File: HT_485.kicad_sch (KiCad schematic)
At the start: 41 parts, among them J1 POWER, J2 485, SW1 EDS05SGRSTR04Q, U1 ISL3179EIBZ, U2 SHT31-DIS-P2.5KS, U3 LM2576D2TR4-3.3G, U4 STM32L010F4P6

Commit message: Adattato master a scatola
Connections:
- net 485+: now also J2.1 (Pin_1); no longer J2.2 (Pin_2)
- net 485-: now also J2.2 (Pin_2); no longer J2.1 (Pin_1)
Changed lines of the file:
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@@
+    (stroke (width 0) (type default) (color 0 0 0 0))
+  )
+  (wire (pts (xy 273.05 132.08) (xy 287.02 132.08))
+    (stroke (width 0) (type default) (color 0 0 0 0))
+  )
+  (wire (pts (xy 125.73 163.83) (xy 125.73 166.37))
+    (stroke (width 0) (type default) (color 0 0 0 0))
+  )
+  (wire (pts (xy 57.15 39.37) (xy 57.15 46.99))
+    (stroke (width 0) (type default) (color 0 0 0 0))
+  )
+  (wire (pts (xy 300.99 119.38) (xy 312.42 119.38))
+    (stroke (width 0) (type default) (color 0 0 0 0))
+  )
+  (wire (pts (xy 189.23 171.45) (xy 189.23 166.37))
+    (stroke (width 0) (type default) (color 0 0 0 0))
+  )
+  (wire (pts (xy 273.05 109.22) (xy 285.75 109.22))
     (stroke (width 0) (type default) (color 0 0 0 0))
   )
   (wire (pts (xy 151.13 119.38) (xy 151.13 124.46))
-    (stroke (width 0) (type default) (color 0 0 0 0))
-  )
-  (wire (pts (xy 273.05 132.08) (xy 287.02 132.08))
-    (stroke (width 0) (type default) (color 0 0 0 0))
-  )
-  (wire (pts (xy 125.73 163.83) (xy 125.73 166.37))
-    (stroke (width 0) (type default) (color 0 0 0 0))
-  )
-  (wire (pts (xy 57.15 39.37) (xy 57.15 46.99))
-    (stroke (width 0) (type default) (color 0 0 0 0))
-  )
-  (wire (pts (xy 300.99 119.38) (xy 312.42 119.38))
-    (stroke (width 0) (type default) (color 0 0 0 0))
-  )
-  (wire (pts (xy 189.23 171.45) (xy 189.23 166.37))
-    (stroke (width 0) (type default) (color 0 0 0 0))
-  )
-  (wire (pts (xy 273.05 109.22) (xy 285.75 109.22))
     (stroke (width 0) (type default) (color 0 0 0 0))
   )
@@
     (pin "2")
   )
-  (symbol (lib_id "Connector:Conn_01x02_Female") (at 156.21 119.38 0) (mirror x) (unit 1)
-    (in_bom yes) (on_board yes) (fields_autoplaced)
-    (property "Reference" "J2" (id 0) (at 155.575 111.76 0))
-    (property "Value" "485" (id 1) (at 155.575 114.3 0))
-    (property "Footprint" "TerminalBlock_Phoenix:TerminalBlock_Phoenix_PT-1,5-2-3.5-H_1x02_P3.50mm_Horizontal" (id 2) (at 156.21 119.38 0)
-      (effects (font (size 1.27 1.27)) hide)
-    )
-    (property "Datasheet" "~" (id 3) (at 156.21 119.38 0)
-      (effects (font (size 1.27 1.27)) hide)
-    )
+  (symbol (lib_id "Connector:Conn_01x02_Female") (at 156.21 116.84 0) (unit 1)
+    (in_bom yes) (on_board yes) (fields_autoplaced)
+    (property "Reference" "J2" (id 0) (at 157.48 116.8399 0)
+      (effects (font (size 1.27 1.27)) (justify left))
+    )
+    (property "Value" "485" (id 1) (at 157.48 119.3799 0)
+      (effects (font (size 1.27 1.27)) (justify left))
+    )
+    (property "Footprint" "TerminalBlock_Phoenix:TerminalBlock_Phoenix_PT-1,5-2-3.5-H_1x02_P3.50mm_Horizontal" (id 2) (at 156.21 116.84 0)
+      (effects (font (size 1.27 1.27)) hide)
+    )
+    (property "Datasheet" "~" (id 3) (at 156.21 116.84 0)
+      (effects (font (size 1.27 1.27)) hide)
+    )

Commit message: Aggiunto terminatore 485
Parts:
- added R20: 120R, Resistor_SMD:R_0805_2012Metric_Pad1.20x1.40mm_HandSolder, symbol Device:R_Small
- added R21, R22: 370R, Resistor_SMD:R_0805_2012Metric_Pad1.20x1.40mm_HandSolder, symbol Device:R_Small
- added SW2: 416131160803, Button_Switch_SMD:SW_DIP_SPSTx03_Slide_KingTek_DSHP03TS_W7.62mm_P1.27mm, symbol Switch:SW_DIP_x03
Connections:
- net +3V3: now also R21.1
- net 485+: now also R20.1, SW2.1, SW2.3
- net 485-: now also R20.2, SW2.2, SW2.4
- net GND: now also R22.2
- new net: R22.1, SW2.5
- new net: R21.2, SW2.6

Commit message: Rivisti dip switch con solder jumper
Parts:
- removed SW1: EDS05SGRSTR04Q, Button_Switch_SMD:SW_DIP_SPSTx05_Slide_KingTek_DSHP05TJ_W5.25mm_P1.27mm_JPin, symbol Switch:SW_DIP_x05
- removed SW2: 416131160803, Button_Switch_SMD:SW_DIP_SPSTx03_Slide_KingTek_DSHP03TS_W7.62mm_P1.27mm, symbol Switch:SW_DIP_x03
- added JP1: BIAS+, Jumper:SolderJumper-2_P1.3mm_Open_RoundedPad1.0x1.5mm, symbol Jumper:SolderJumper_2_Open
- added JP2: BIAS-, Jumper:SolderJumper-2_P1.3mm_Open_RoundedPad1.0x1.5mm, symbol Jumper:SolderJumper_2_Open
- added JP3: TERMINATOR, Jumper:SolderJumper-2_P1.3mm_Open_RoundedPad1.0x1.5mm, symbol Jumper:SolderJumper_2_Open
- added JP4: A1, Jumper:SolderJumper-2_P1.3mm_Open_RoundedPad1.0x1.5mm, symbol Jumper:SolderJumper_2_Open
- added JP5: A3, Jumper:SolderJumper-2_P1.3mm_Open_RoundedPad1.0x1.5mm, symbol Jumper:SolderJumper_2_Open
- added JP6: A5, Jumper:SolderJumper-2_P1.3mm_Open_RoundedPad1.0x1.5mm, symbol Jumper:SolderJumper_2_Open
- added JP7: A2, Jumper:SolderJumper-2_P1.3mm_Open_RoundedPad1.0x1.5mm, symbol Jumper:SolderJumper_2_Open
- added JP8: A4, Jumper:SolderJumper-2_P1.3mm_Open_RoundedPad1.0x1.5mm, symbol Jumper:SolderJumper_2_Open
- R20: value 120R -> 370R
- R22: value 370R -> 120R
- U2: value SHT31-DIS-P2.5KS -> SHT31-DIS + SF2; footprint Sensor_Humidity:Sensirion_DFN-8-1EP_2.5x2.5mm_P0.5mm_EP1.1x1.7mm -> HT485:Sensirion_DFN-8-1EP_2.5x2.5mm_P0.5mm_EP1.1x1.7mm
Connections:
- net +3V3: now also R20.1; no longer R21.1
- net 485+: now also JP1.1 (A), JP3.2 (B); no longer R20.1
- net 485-: now also R22.2, JP2.1 (A); no longer R20.2
- net GND: now also R21.2, JP4.2 (B), JP5.2 (B), JP6.2 (B), JP7.2 (B), JP8.2 (B); no longer R22.2
- net at R12.1, R17.2: now also JP8.1 (A)
- net at R22.1: now also JP3.1 (A)
- net at R13.1, R18.2: now also JP6.1 (A)
- net at R11.1, R16.2: now also JP5.1 (A)
- net at R14.2, R9.1: now also JP4.1 (A)
- net at R10.1, R15.2: now also JP7.1 (A)
- new net: JP1.2 (B), R20.2
- new net: JP2.2 (B), R21.1

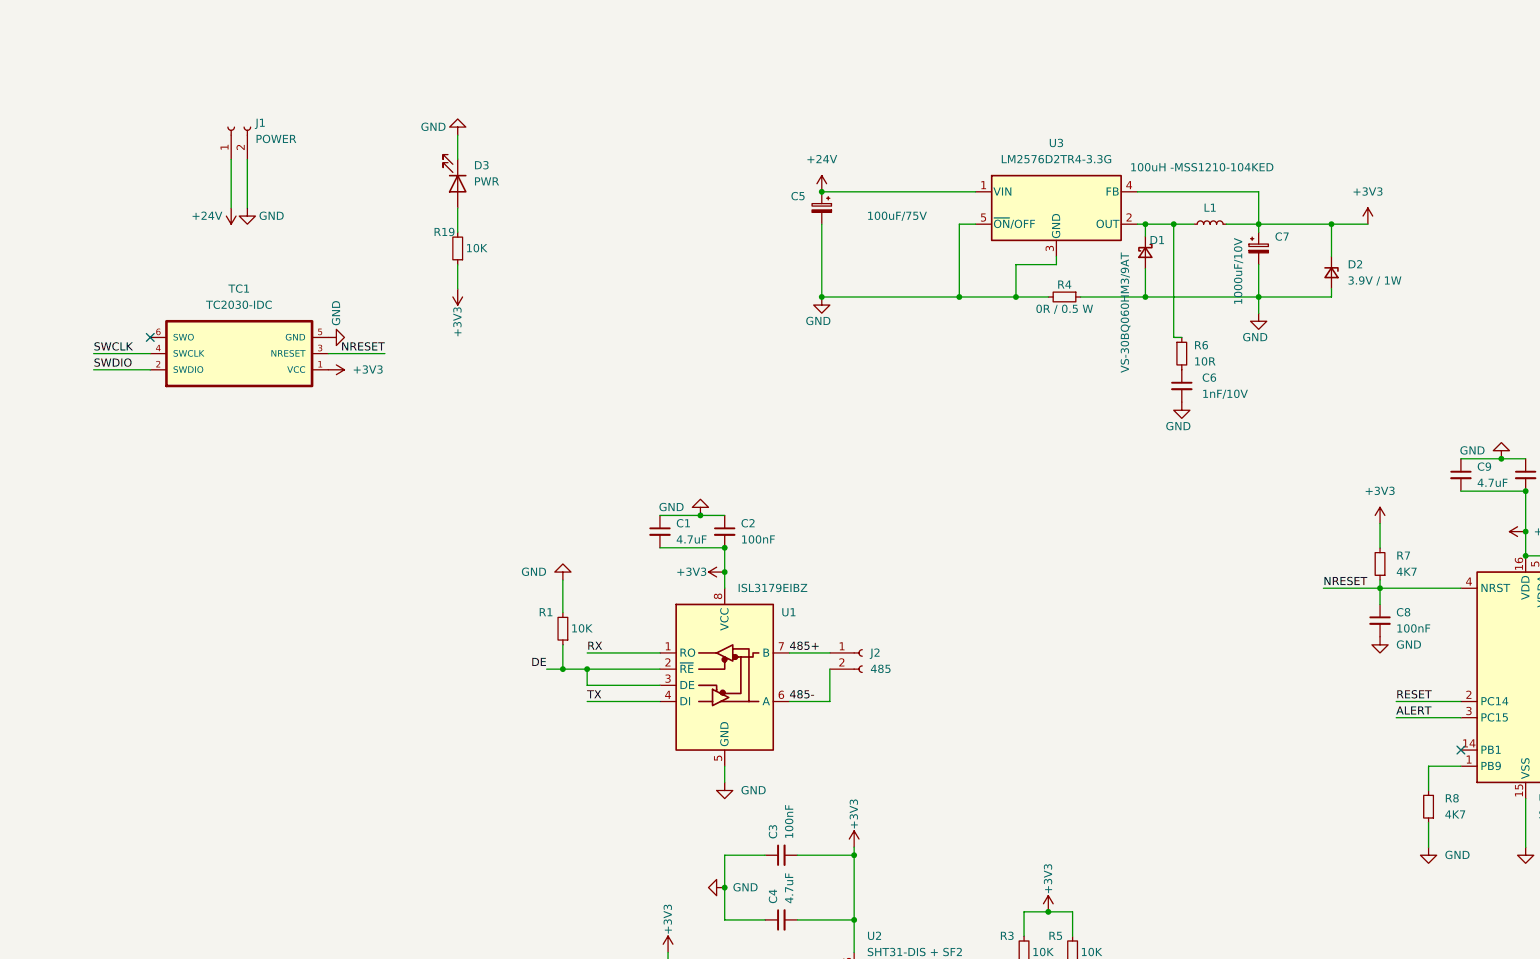
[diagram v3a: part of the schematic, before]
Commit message: Messa pompa di carica per 485 a 5V
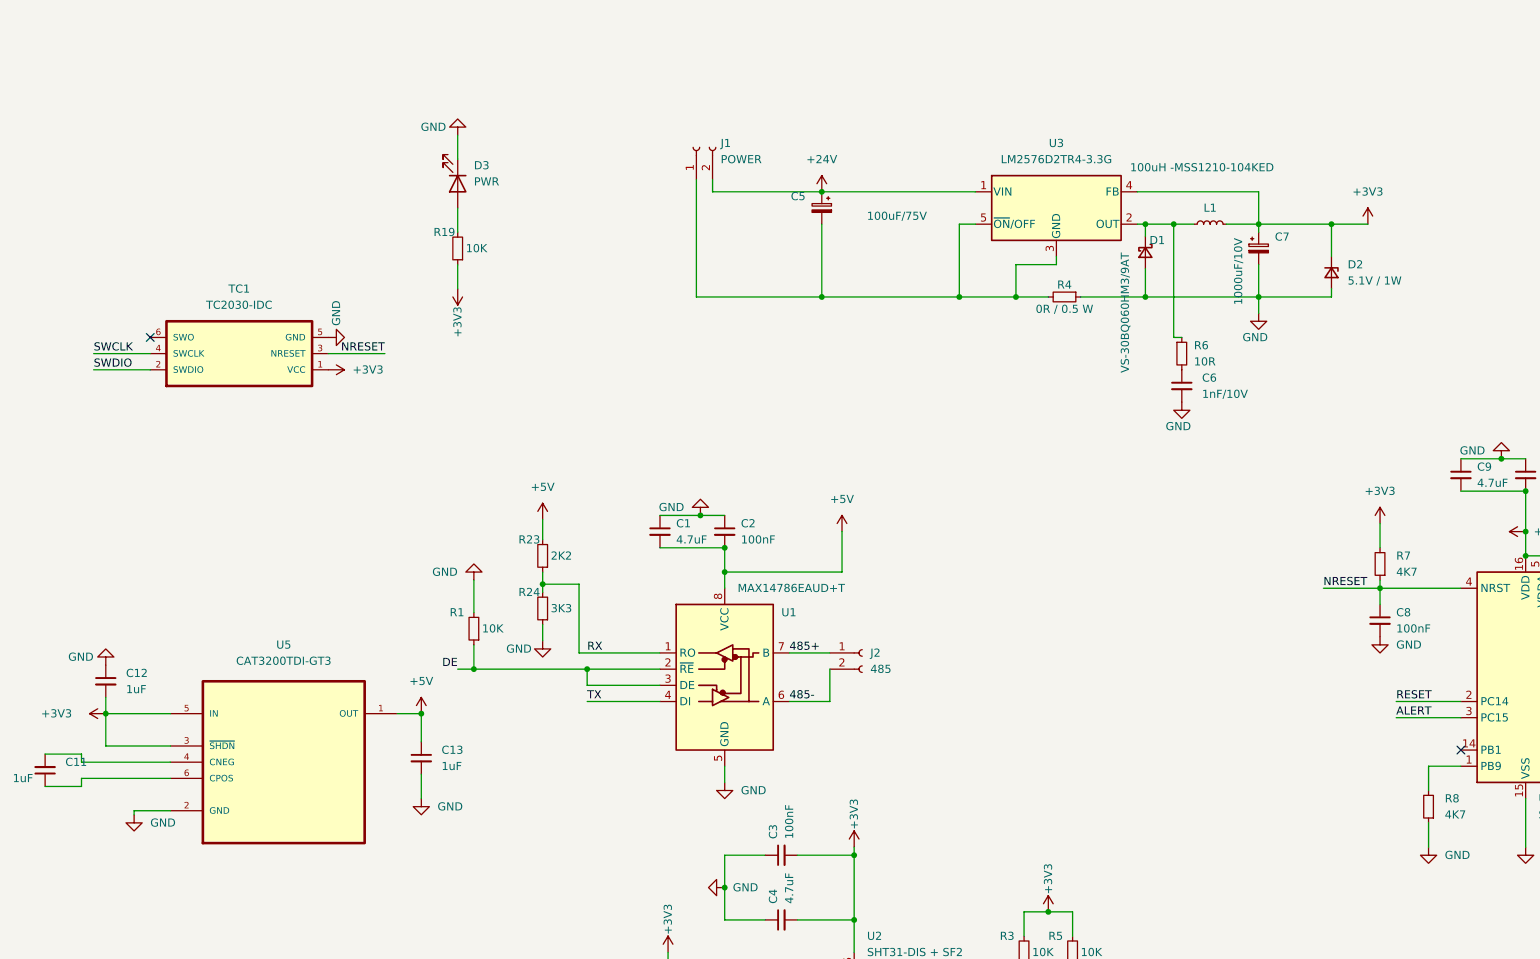
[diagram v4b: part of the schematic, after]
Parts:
- added C11, C12, C13: 1uF, Capacitor_SMD:C_0805_2012Metric_Pad1.18x1.45mm_HandSolder, symbol Device:C_Small
- added R23: 2K2, Resistor_SMD:R_0805_2012Metric_Pad1.20x1.40mm_HandSolder, symbol Device:R_Small
- added R24: 3K3, Resistor_SMD:R_0805_2012Metric_Pad1.20x1.40mm_HandSolder, symbol Device:R_Small
- added U5: CAT3200TDI-GT3, Package_TO_SOT_SMD:TSOT-23-6, symbol HT485:CAT3200TDI-GT3
- D2: value 3.9V / 1W -> 5.1V / 1W
- U1: value ISL3179EIBZ -> MAX14786EAUD+T
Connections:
- net +24V: now also J1.2 (Pin_2); no longer J1.1 (Pin_1)
- net +3V3: now also C12.2, U5.3 (~{SHDN}), U5.5 (IN); no longer C1.2, C2.2, U1.8 (VCC)
- net GND: now also C12.1, C13.2, R24.1, U5.2 (GND); no longer C5.2, J1.2 (Pin_2), R4.2, U3.3 (GND), U3.5 (~{ON}/OFF)
- net RX: now also R23.1, R24.2
- new net: C5.2, J1.1 (Pin_1), R4.2, U3.3 (GND), U3.5 (~{ON}/OFF)
- new net: C11.1, U5.6 (CPOS)
- new net: C11.2, U5.4 (CNEG)
- new net +5V: C1.2, C13.1, C2.2, R23.2, U1.8 (VCC), U5.1 (OUT)
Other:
- moved on the sheet: J1, R1

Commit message: Revisione 1.0.0.0 con PT1000
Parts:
- removed C10: 100nF, Capacitor_SMD:C_0805_2012Metric_Pad1.18x1.45mm_HandSolder, symbol Device:C_Small
- removed JP4: A1, Jumper:SolderJumper-2_P1.3mm_Open_RoundedPad1.0x1.5mm, symbol Jumper:SolderJumper_2_Open
- removed JP5: A3, Jumper:SolderJumper-2_P1.3mm_Open_RoundedPad1.0x1.5mm, symbol Jumper:SolderJumper_2_Open
- removed JP6: A5, Jumper:SolderJumper-2_P1.3mm_Open_RoundedPad1.0x1.5mm, symbol Jumper:SolderJumper_2_Open
- removed JP7: A2, Jumper:SolderJumper-2_P1.3mm_Open_RoundedPad1.0x1.5mm, symbol Jumper:SolderJumper_2_Open
- removed JP8: A4, Jumper:SolderJumper-2_P1.3mm_Open_RoundedPad1.0x1.5mm, symbol Jumper:SolderJumper_2_Open
- removed TC1: TC2030-IDC, TC2030:TC2030-IDC, symbol TC2030:TC2030-IDC
- removed U2: SHT31-DIS + SF2, HT485:Sensirion_DFN-8-1EP_2.5x2.5mm_P0.5mm_EP1.1x1.7mm, symbol Sensor_Humidity:SHT31-DIS
- removed U4: STM32L010F4P6, Package_SO:TSSOP-20_4.4x6.5mm_P0.65mm, symbol MCU_ST_STM32L0:STM32L011F3Px
- added C14, C15, C20: 100nF, Capacitor_SMD:C_0805_2012Metric, symbol Device:C_Small
- added C16: 1nF, Capacitor_SMD:C_0805_2012Metric, symbol Device:C_Small
- added C17: 1uF/25V, Capacitor_SMD:C_0805_2012Metric, symbol Device:C_Small
- added C18, C19: 100uF/25V, Capacitor_SMD:CP_Elec_6.3x7.7, symbol Device:C_Polarized_Small
- added D10: STPS0520Z, Diode_SMD:D_SOD-123, symbol Device:D_Schottky_Small
- added D4, D5, D6, D7, D8: 1N4148WS, Diode_SMD:D_SOD-323, symbol Diode:1N4148WS
- added D9: BAV99, Package_TO_SOT_SMD:SOT-23, symbol Diode:BAV99
- added J3: PT1000, TerminalBlock_Phoenix:TerminalBlock_Phoenix_PT-1,5-2-3.5-H_1x02_P3.50mm_Horizontal, symbol Connector:Conn_01x02_Female
- added J4: H/T Sensor, Connector_JST:JST_PH_S6B-PH-SM4-TB_1x06-1MP_P2.00mm_Horizontal, symbol Connector:Conn_01x06_Female
- added J5: PRG, Connector_PinSocket_2.54mm:PinSocket_2x03_P2.54mm_Vertical, symbol Connector_Generic:Conn_02x03_Odd_Even
- added JP4: UART_BOOT_MSG, Jumper:SolderJumper-3_P1.3mm_Bridged12_RoundedPad1.0x1.5mm_NumberLabels, symbol Jumper:SolderJumper_3_Bridged12
- added Q1, Q2, Q3, Q4: BC817, Package_TO_SOT_SMD:SOT-23, symbol Transistor_BJT:BC817
- added R25, R26, R27, R30, R31: 10K, Resistor_SMD:R_0805_2012Metric_Pad1.20x1.40mm_HandSolder, symbol Device:R_Small
- added R28, R29: 0R, Resistor_SMD:R_0805_2012Metric_Pad1.20x1.40mm_HandSolder, symbol Device:R_Small
- added TP1: D+, TestPoint:TestPoint_Pad_D1.0mm, symbol Connector:TestPoint
- added TP2: D-, TestPoint:TestPoint_Pad_D1.0mm, symbol Connector:TestPoint
- added U2: TL082, Package_SO:SOIC-8-1EP_3.9x4.9mm_P1.27mm_EP2.29x3mm, symbol Amplifier_Operational:TL082
- added U4: ESP32-S3-WROOM-1-N16R8, Espressif:ESP32-S3-WROOM-1, symbol Espressif:ESP32-S3-WROOM-1
- added U6: L7815, Package_TO_SOT_SMD:TO-263-2, symbol Regulator_Linear:L7815
- C1, C11, C12, C13, C2, C8: footprint Capacitor_SMD:C_0805_2012Metric_Pad1.18x1.45mm_HandSolder -> Capacitor_SMD:C_0805_2012Metric
- C3: value 100nF -> 1uF/16V; footprint Capacitor_SMD:C_0805_2012Metric_Pad1.18x1.45mm_HandSolder -> Capacitor_SMD:C_0805_2012Metric
- C4: value 4.7uF -> 100nF; footprint Capacitor_SMD:C_0805_2012Metric_Pad1.18x1.45mm_HandSolder -> Capacitor_SMD:C_0805_2012Metric
- C5: value 100uF/75V -> 100uF / 50V; footprint Capacitor_SMD:CP_Elec_10x10 -> Capacitor_SMD:CP_Elec_8x10.5
- C9: value 4.7uF -> 10uF; footprint Capacitor_SMD:C_0805_2012Metric_Pad1.18x1.45mm_HandSolder -> Capacitor_SMD:C_0805_2012Metric
- D2: value 5.1V / 1W -> 3.9V/1W; footprint Diode_SMD:D_SOD-128 -> Diode_SMD:D_SMA
- R10: value 1K -> 100R
- R11: value 1K -> 10K
- R15: value 10K -> 1K
- R16: value 10K -> 10R
- R17: value 10K -> 3k3
- R2: value 10K -> 1K 1%
- R23: value 2K2 -> 4K7
- R24: value 3K3 -> 10K
- R7, R8: value 4K7 -> 10K
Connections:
- net +24V: now also U6.1 (IN)
- net +3V3: now also C8.1, C9.1, R23.2, D9.2 (A), J4.1 (Pin_1), J5.1 (Pin_1), R26.2, R27.2, R31.1, U4.2 (3V3); no longer C3.2, C4.2, C9.2, R14.1, R15.1, R16.1, R17.1, R18.1, R2.2, R3.2, R5.2
- net +5V: no longer R23.2
- net 485+: now also J2.2 (Pin_2); no longer J2.1 (Pin_1)
- net 485-: now also J2.1 (Pin_1); no longer J2.2 (Pin_2)
- net ALERT: now also J4.5 (Pin_5), U4.15 (GPIO3/TOUCH3/ADC1_CH2)
- net DE: now also U4.4 (GPIO4/TOUCH4/ADC1_CH3)
- net GND: now also C3.2, C4.2, C9.2, R13.2, R16.2, R5.2, C14.2, C15.2, C19.1, C20.2, D5.2 (A), D9.1 (K), J3.2 (Pin_2), J4.6 (Pin_6), J5.6 (Pin_6), Q1.2 (E), R25.2, R30.2, U4.1 (GND), U4.40 (GND), U4.41 (GND); no longer C3.1, C4.1, C9.1, R24.1, R8.1
- net RESET: now also J4.4 (Pin_4), U4.38 (GPIO2/TOUCH2/ADC1_CH1); no longer R2.1
- net RX: now also D10.2 (A), U4.11 (GPIO18/U1RXD/ADC2_CH7/CLK_OUT3); no longer R24.2, U1.1 (RO)
- net SCL: now also J4.2 (Pin_2), R26.1, U4.25 (GPIO48/SPICLK_N/SUBSPICLK_N_DIFF); no longer R5.1
- net SDA: now also J4.3 (Pin_3), R27.1, U4.24 (GPIO47/SPICLK_P/SUBSPICLK_P_DIFF); no longer R3.1
- net TX: now also U4.10 (GPIO17/U1TXD/ADC2_CH6)
- net at R8.2: now also Q3.1 (B)
- net at R10.2: now also C16.2
- net at R11.2: now also D6.1 (K), Q1.3 (C), Q2.1 (B)
- net at R12.2: now also R13.1, R15.1
- net OP_NEG_V_PWM: now reaches R9.2
- net OP_NEG_V_PWM: now also R5.1, C16.1, U4.5 (GPIO5/TOUCH5/ADC1_CH4)
- net +15V: now reaches R11.1
- net +15V: now also C4.1, R12.1, R2.1, C17.1, D4.1 (K), Q2.3 (C), U2.8 (V+), U6.3 (OUT); no longer R16.2
- net at R17.2: now also R18.1, U2.7; no longer R12.1
- net at R15.2: now also R17.1, U2.6 (-); no longer R10.1
- net PT1000_ADC: now reaches R18.2
- net PT1000_ADC: now also C20.1, D9.3 (K), R25.1, U4.39 (GPIO1/TOUCH1/ADC1_CH0); no longer R13.1
- net at R14.2: now also U2.1, U2.2 (-); no longer R9.1
- net NRESET renamed EN
- net EN: now also C3.1, R28.2, U4.3 (EN); no longer C8.1
- new net: Q4.3 (C), R29.1
- new net: R14.1, U2.5 (+)
- new net: Q3.3 (C), R28.1
- new net: C18.1, D7.2 (A), D8.1 (K)
- new net: C18.2, D6.2 (A), Q2.2 (E)
- new net: C17.2, U6.2 (GND)
- new net: J3.1 (Pin_1), R2.2, R3.2
- new net: C15.1, D4.2 (A), D5.1 (K), R3.1, U2.3 (+)
- new net: Q1.1 (B), R10.1, R9.1
- new net: JP4.2 (C), U4.16 (GPIO46)
- new net: JP4.1 (A), R30.1
- new net: D10.1 (K), U1.1 (RO)
- new net: Q4.1 (B), R24.2
- new net: JP4.3 (B), R31.2
- new net: D7.1 (K), R16.1
- new net -12V: C14.1, C19.2, D8.2 (A), U2.4 (V-)
- new net D+: TP1.1, U4.14 (GPIO20/U1CTS/ADC2_CH9/CLK_OUT1/USB_D+)
- new net D-: TP2.1, U4.13 (GPIO19/U1RTS/ADC2_CH8/CLK_OUT2/USB_D-)
- new net DTR: J5.4 (Pin_4), Q4.2 (E), R8.1
- new net GPIO0: R29.2, U4.27 (GPIO0/BOOT)
- new net RTS: J5.5 (Pin_5), Q3.2 (E), R24.1
- new net U0RXD: J5.2 (Pin_2), U4.36 (U0RXD/GPIO44/CLK_OUT2)
- new net U0TXD: J5.3 (Pin_3), U4.37 (U0TXD/GPIO43/CLK_OUT1)
- no-connect marks 2 -> 21
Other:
- note added: "485"
- note added: "Auto program DTR RTS -> EN IO0 IO2 1 1 1 1 1 0 0 1 1 1 1 0 0 1 1 0 1 1 0 0"
- note added: "MCUì"
- note added: "POWER OUT: SWITCHING 3.3V 3A LDO +15V 1.5A CHARGING PUMP -12V 0.15A VIA MCU PWM AT 10 kHZ CHARGING PUMP +5V"
- note added: "PT1000 Fondoscala 0-200 °C Sengale da 0 a 3.3"
- note added: "SHT31 CONNECTOR"
- moved on the sheet: C1, C11, C12, C13, C2, C5, C6, C7, D1, D2, D3, J1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

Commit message: Remaster
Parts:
- removed C11, C12, C13: 1uF, Capacitor_SMD:C_0805_2012Metric, symbol Device:C_Small
- removed R4: 0R / 0.5 W, Resistor_SMD:R_1210_3225Metric, symbol Device:R_Small
- removed U5: CAT3200TDI-GT3, Package_TO_SOT_SMD:TSOT-23-6, symbol HT485:CAT3200TDI-GT3
- added C?: 1uF/25V, Capacitor_SMD:C_0805_2012Metric, symbol Device:C_Small
- added U?: L7815, Package_TO_SOT_SMD:TO-263-2, symbol Regulator_Linear:L7815
- added U?: L7805, symbol Regulator_Linear:L7805
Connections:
- net +15V: now also C?.1, U?.3 (OUT)
- net +24V: now also U?.1 (IN)
- net GND: now also C17.2, C5.2, J1.1 (Pin_1), U3.3 (GND), U3.5 (~{ON}/OFF), U6.2 (GND), C?.2, U?.2 (GND)
